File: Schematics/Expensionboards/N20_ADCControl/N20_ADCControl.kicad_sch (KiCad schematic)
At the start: 36 parts

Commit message: Schematic-analyses N20
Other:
- note added: "Gated Counter-overflow"
- note added: "Invert counterpulses"
- note removed: "Signals for uP: counter-overflow"
- note removed: "uP-counterpulses invert"
- moved on the sheet: D2004B, D2004C, D2004D, D2005A, D2005B, D2010C

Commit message: More N20
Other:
- note added: "Counter-control"
- note added: "xECP = Enable Counter Pulses (to Counter) xSCP = Stop Counter Pulses xRDY = Measurement Ready xEC20 = ? xXC20 = Counter Overflow (pulse, 1.40us) xENC20 = ? xEC20 = Enable CounterOverflow gate xERD = Gate for XC20->uP xSTD = ? xRD! = ?"
- note removed: "Signals for counter (gated clockpulses, reset)"
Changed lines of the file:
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@@
+		)
+	)
+	(text "xECP   = Enable Counter Pulses (to Counter)\nxSCP   = Stop Counter Pulses\nxRDY   = Measurement Ready\nxEC20  = ?\nxXC20  = Counter Overflow (pulse, 1.40us)\nxENC20 = ?\nxEC20  = Enable CounterOverflow gate\nxERD   = Gate for XC20->uP\nxSTD   = ?\n\nxRD!   = ?"
+		(exclude_from_sim no)
+		(at 254.254 114.808 0)
+		(effects
+			(font
+				(size 1.27 1.27)
+			)
+			(justify left top)
 		)
 	)
@@
 		)
 	)
-	(text "Signals for counter (gated clockpulses, reset)"
+	(text "Counter-control"
 		(exclude_from_sim no)
 		(at 63.246 18.542 0)

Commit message: More N20
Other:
- note removed: "xECP = Enable Counter Pulses (to Counter) xSCP = Stop Counter Pulses xRDY = Measurement Ready xEC20 = ? xXC20 = Counter Overflow (pulse, 1.40us) xENC20 = ? xEC20 = Enable CounterOverflow gate xERD = Gate for XC20->uP xSTD = ? xRD! = ?"
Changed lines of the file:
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@@
 	(title_block
 		(title "Philips PM2528 - N20 (ADC Control)")
-		(date "2025-12-16")
+		(date "2026-01-13")
 		(rev "1.0")
 		(company "D. Kupers")
@@
 		)
 	)
-	(text "xECP   = Enable Counter Pulses (to Counter)\nxSCP   = Stop Counter Pulses\nxRDY   = Measurement Ready\nxEC20  = ?\nxXC20  = Counter Overflow (pulse, 1.40us)\nxENC20 = ?\nxEC20  = Enable CounterOverflow gate\nxERD   = Gate for XC20->uP\nxSTD   = ?\n\nxRD!   = ?"
-		(exclude_from_sim no)
-		(at 254.254 114.808 0)
-		(effects
-			(font
-				(size 1.27 1.27)
-			)
-			(justify left top)
-		)
-	)
 	(text "Invert counterpulses"
 		(exclude_from_sim no)
@@
 	(wire
 		(pts
-			(xy 71.12 119.38) (xy 76.2 119.38)
+			(xy 46.99 119.38) (xy 76.2 119.38)
 		)
 		(stroke
@@
 	)
 	(label "RC"
-		(at 71.12 119.38 0)
+		(at 46.99 119.38 0)
 		(effects
 			(font

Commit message: More N20
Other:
- note added: "Detect Rampup-end, Rampdown, polarity (to ADC)"
- note added: "Gated Counter-overflow (to uP)"
- note added: "Rampup, Autozero (to ADC)"
- note removed: "Gated Counter-overflow"
- note removed: "Signals for ADC: Detect Rampup-end, Rampdown, polarity"
- note removed: "Signals for ADC: Rampup, Autozero"
- moved on the sheet: D2010B, D2010D
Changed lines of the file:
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@@
 	(title_block
 		(title "Philips PM2528 - N20 (ADC Control)")
-		(date "2026-01-13")
+		(date "2026-01-14")
 		(rev "1.0")
 		(company "D. Kupers")
@@
 	(rectangle
 		(start 63.5 82.55)
-		(end 194.31 128.27)
+		(end 194.31 127)
 		(stroke
 			(width 0)
@@
 		)
 	)
-	(text "Signals for ADC: Rampup, Autozero"
+	(text "Rampup, Autozero (to ADC)"
 		(exclude_from_sim no)
 		(at 63.5 80.518 0)
@@
 		)
 	)
-	(text "Signals for ADC: Detect Rampup-end, Rampdown, polarity"
+	(text "Detect Rampup-end, Rampdown, polarity (to ADC)"
 		(exclude_from_sim no)
 		(at 63.246 134.874 0)
@@
 		)
 	)
-	(text "Gated Counter-overflow"
+	(text "Gated Counter-overflow (to uP)"
 		(exclude_from_sim no)
 		(at 63.5 229.616 0)
@@
 	(wire
 		(pts
-			(xy 95.25 106.68) (xy 95.25 109.22)
+			(xy 95.25 104.14) (xy 95.25 109.22)
 		)
 		(stroke
@@
 	(wire
 		(pts
-			(xy 91.44 116.84) (xy 95.25 116.84)
+			(xy 91.44 114.3) (xy 99.06 114.3)
 		)
 		(stroke
@@
 	(wire
 		(pts
-			(xy 46.99 119.38) (xy 76.2 119.38)
-		)
-		(stroke
-			(width 0)
-			(type default)
-		)
-	)
-	(wire
-		(pts
 			(xy 22.86 31.75) (xy 27.94 31.75)
 		)
@@
 	(wire
 		(pts
-			(xy 71.12 104.14) (xy 76.2 104.14)
+			(xy 71.12 101.6) (xy 76.2 101.6)
 		)
 		(stroke
@@
 	(wire
 		(pts
-			(xy 140.97 99.06) (xy 146.05 99.06)
+			(xy 138.43 99.06) (xy 146.05 99.06)
 		)
 		(stroke
@@
 	(wire
 		(pts
-			(xy 46.99 85.09) (xy 140.97 85.09)
+			(xy 46.99 86.36) (xy 138.43 86.36)
 		)
 		(stroke
@@
 	(wire
 		(pts
-			(xy 67.31 114.3) (xy 76.2 114.3)
+			(xy 67.31 111.76) (xy 76.2 111.76)
 		)
 		(stroke
@@
 	(wire
 		(pts
-			(xy 106.68 96.52) (xy 106.68 104.14)
+			(xy 106.68 90.17) (xy 106.68 104.14)
 		)
 		(stroke
@@
 	(wire
 		(pts
-			(xy 67.31 93.98) (xy 67.31 114.3)
+			(xy 67.31 93.98) (xy 67.31 111.76)
 		)
 		(stroke
@@
 	(wire
 		(pts
-			(xy 91.44 106.68) (xy 95.25 106.68)
+			(xy 91.44 104.14) (xy 95.25 104.14)
 		)
 		(stroke
@@
 	(wire
 		(pts
+			(xy 46.99 116.84) (xy 76.2 116.84)
+		)
+		(stroke
+			(width 0)
+			(type default)
+		)
+	)
+	(wire
+		(pts
 			(xy 184.15 210.82) (xy 189.23 210.82)
 		)
@@
 	(wire
 		(pts
-			(xy 95.25 116.84) (xy 95.25 114.3)
-		)
-		(stroke
-			(width 0)
-			(type default)
-		)
-	)
-	(wire
-		(pts
 			(xy 95.25 179.07) (xy 135.89 179.07)
 		)
@@
 	(wire
 		(pts
-			(xy 95.25 114.3) (xy 99.06 114.3)
-		)
-		(stroke
-			(width 0)
-			(type default)
-		)
-	)
-	(wire
-		(pts
 			(xy 67.31 176.53) (xy 71.12 176.53)
 		)
@@
 	(wire
 		(pts
-			(xy 71.12 109.22) (xy 76.2 109.22)
+			(xy 71.12 106.68) (xy 76.2 106.68)
 		)
 		(stroke
@@
 	(wire
 		(pts
-			(xy 140.97 85.09) (xy 140.97 99.06)
+			(xy 138.43 86.36) (xy 138.43 99.06)
 		)
 		(stroke
@@
 	(wire
 		(pts
-			(xy 46.99 96.52) (xy 106.68 96.52)
+			(xy 46.99 90.17) (xy 106.68 90.17)
 		)
 		(stroke
@@
 	)
 	(label "CP"
-		(at 46.99 85.09 0)
+		(at 46.99 86.36 0)
 		(effects
 			(font
@@
 	)
 	(label "SAZ"
-		(at 46.99 96.52 0)
+		(at 46.99 90.17 0)
 		(effects
 			(font
@@
 	)
 	(label "x~{RD}"
-		(at 71.12 109.22 0)
+		(at 71.12 106.68 0)
 		(effects
 			(font
@@
 	)
 	(label "xRDY"
-		(at 71.12 104.14 0)
+		(at 71.12 101.6 0)
 		(effects
 			(font
@@
 	)
 	(label "RC"
-		(at 46.99 119.38 0)
+		(at 46.99 116.84 0)
 		(effects
 			(font
@@
 	(symbol
 		(lib_id "4xxx:4081")
-		(at 83.82 116.84 0)
+		(at 83.82 114.3 0)
 		(unit 4)
 		(exclude_from_sim no)
@@
 		(dnp no)
 		(property "Reference" "D2010"
-			(at 83.82 122.936 0)
+			(at 83.82 120.396 0)
 			(effects
 				(font
@@
 		)
 		(property "Value" "HEF4081"
-			(at 83.82 125.476 0)
+			(at 83.82 122.936 0)
 			(effects
 				(font
@@
 		)
 		(property "Footprint" "Package_DIP:DIP-14_W7.62mm"
-			(at 83.82 116.84 0)
+			(at 83.82 114.3 0)
 			(effects
 				(font
@@
 		)
 		(property "Datasheet" "http://www.intersil.com/content/dam/Intersil/documents/cd40/cd4073bms-81bms-82bms.pdf"
-			(at 83.82 116.84 0)
+			(at 83.82 114.3 0)
 			(effects
 				(font
@@
 		)
 		(property "Description" "Quad And 2 inputs"
-			(at 83.82 116.84 0)
+			(at 83.82 114.3 0)
 			(effects
 				(font
@@
 	(symbol
 		(lib_id "4xxx:4081")
-		(at 83.82 106.68 0)
+		(at 83.82 104.14 0)
 		(unit 2)
 		(exclude_from_sim no)
@@
 		(on_board yes)
 		(dnp no)
-		(fields_autoplaced yes)
 		(property "Reference" "D2010"
-			(at 83.8117 97.79 0)
+			(at 84.074 96.012 0)
 			(effects
 				(font
@@
 		)
 		(property "Value" "HEF4081"
-			(at 83.8117 100.33 0)
+			(at 84.074 98.552 0)
 			(effects
 				(font
@@
 		)
 		(property "Footprint" "Package_DIP:DIP-14_W7.62mm"
-			(at 83.82 106.68 0)
+			(at 83.82 104.14 0)
 			(effects
 				(font
@@
 		)
 		(property "Datasheet" "http://www.intersil.com/content/dam/Intersil/documents/cd40/cd4073bms-81bms-82bms.pdf"
-			(at 83.82 106.68 0)
+			(at 83.82 104.14 0)
 			(effects
 				(font
@@
 		)
 		(property "Description" "Quad And 2 inputs"
-			(at 83.82 106.68 0)
+			(at 83.82 104.14 0)
 			(effects
 				(font
@@
 		(on_board yes)
 		(dnp no)
-		(fields_autoplaced yes)
 		(property "Reference" "D2010"
-			(at 129.5317 87.63 0)
+			(at 129.0403 88.392 0)
 			(effects
 				(font
@@
 		)
 		(property "Value" "HEF4081"
-			(at 129.5317 90.17 0)
+			(at 129.794 90.678 0)
 			(effects
 				(font

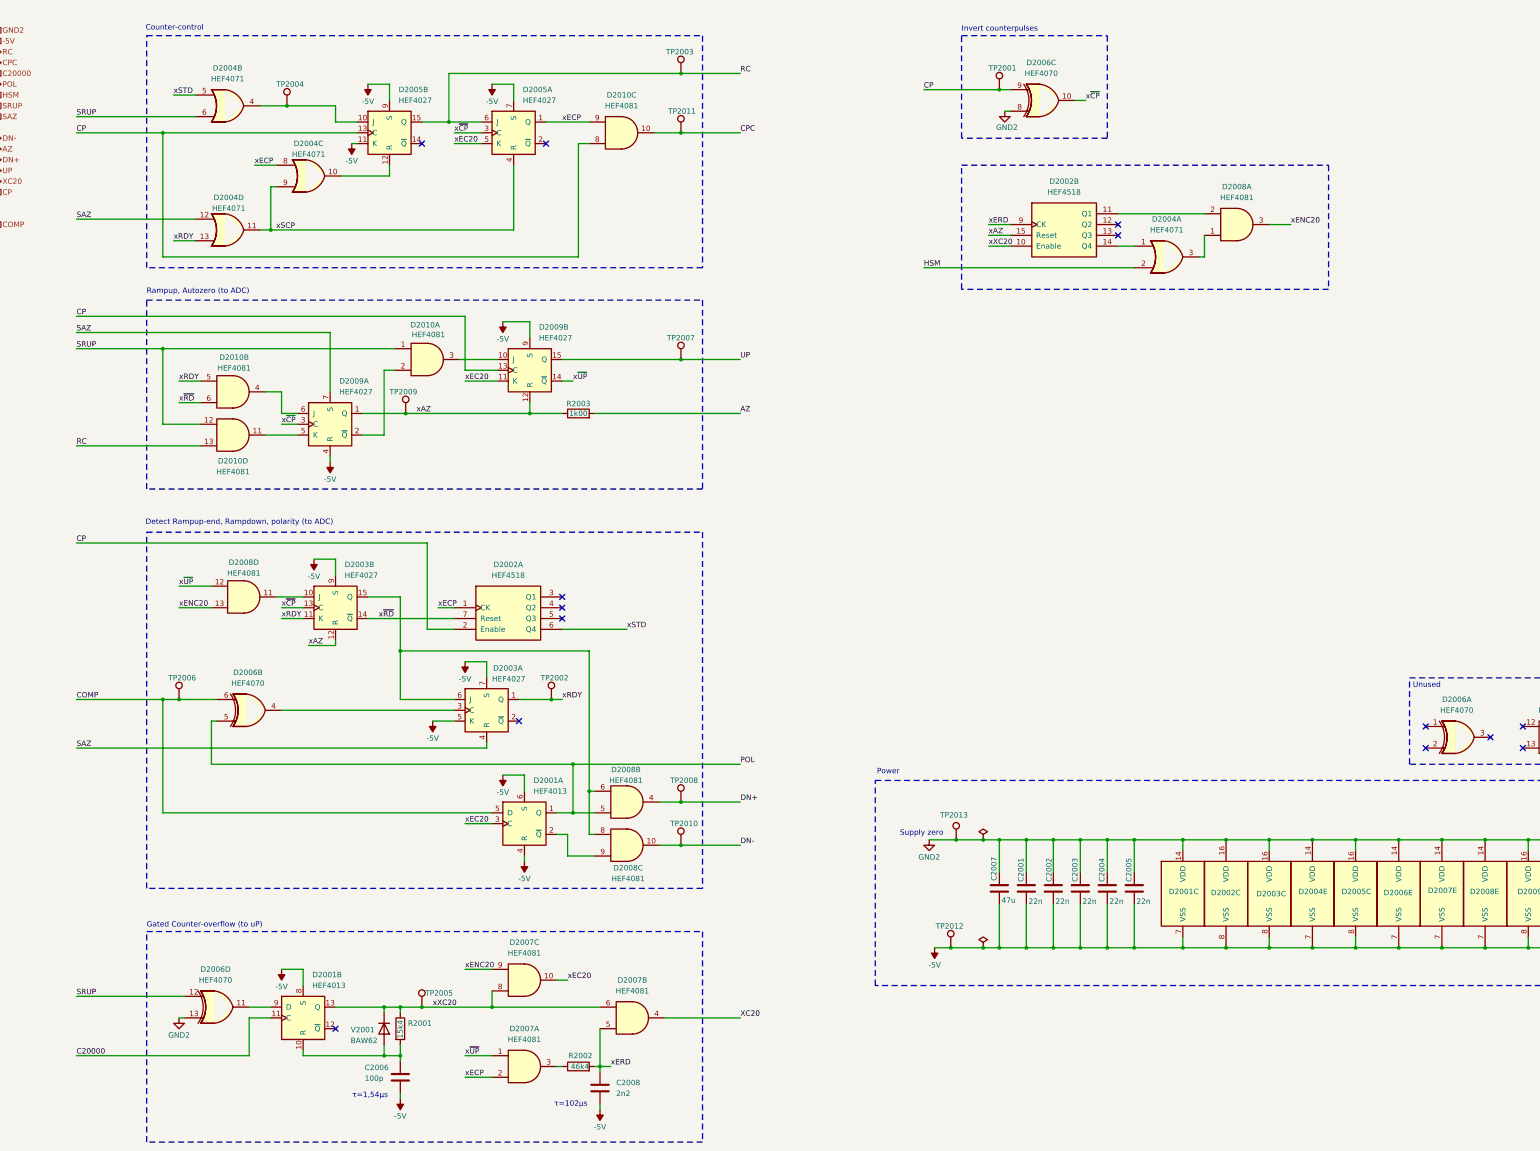
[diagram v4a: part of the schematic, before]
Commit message: More N20, update Ghidra-project to most recent Ghidra version
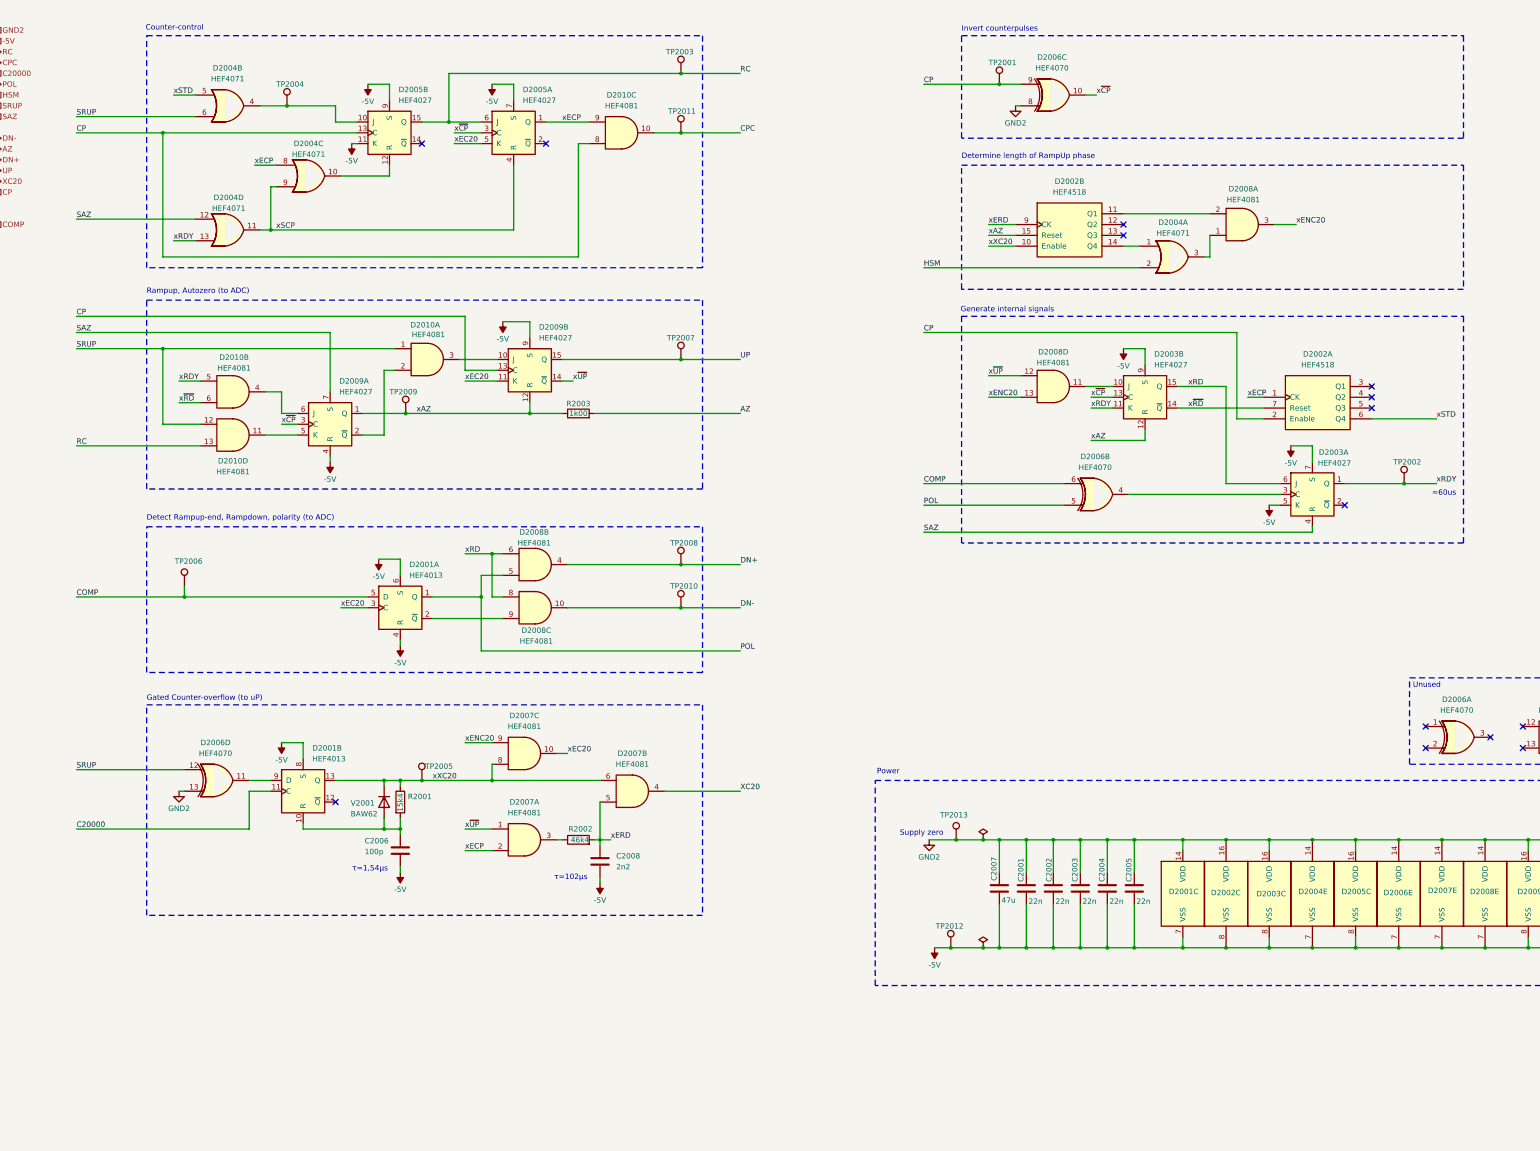
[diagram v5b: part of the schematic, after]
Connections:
- net xRD: now reaches D2003.15 (Q), D2003.6 (J), D2008.6, D2008.8
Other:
- note added: "Determine length of RampUp phase"
- note added: "Generate internal signals"
- note added: "≈60us"
- moved on the sheet: C2006, C2008, D2001A, D2001B, D2002A, D2002B, D2003A, D2003B, D2004A, D2006B, D2006C, D2006D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
